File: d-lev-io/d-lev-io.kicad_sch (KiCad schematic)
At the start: 48 parts, among them J1 USB_C_Receptacle_USB2.0, J2 PJ-059A, J3 Conn_01x12_MountingPin, J4 MIDI_OUT_JACK, U3 ADP151-3.3, U6 74AHC1G126

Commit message: io board more analog schematic capture
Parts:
- added J6: HEADPHONE, Connector_Audio:Jack_3.5mm_CUI_SJ-3523-SMT_Horizontal, symbol Connector:AudioJack3
- added R42, R44: 0, Resistor_SMD:R_0603_1608Metric, symbol Device:R_Small
- added RV2: VOL_POT, symbol Device:R_Potentiometer_MountingPin
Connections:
- net +3V3: now also RV2.1
- net GND: now also RV2.3, RV2.MP (MountPin)
- new net: J6.R, R42.1
- new net: J6.T, R44.1
- new net OUT_SE.G: J6.S, R42.2, R44.2
- new net SAMD11/VOLUME_POT: RV2.2
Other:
- sheet DAC ports: added DAC_GPIO, DAC_RESET, HPA_SHDN, OUT_SE{L,R,G}; removed DAC{GPIO,RESET}, OUT_BAL{L+,L-,R+,R-}
- sheet SAMD11 ports: added ESS_GPIO, HPA_SHDN, VOLUME_POT; removed none
- note added: "hpa: MAX97220C/E"
- note removed: "hpa: MAX97220A"
- moved on the sheet: C21, C22, TP4, U3

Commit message: many board updates
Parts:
- removed JP3: JUMP_VBUCK, Jumper:SolderJumper-2_P1.3mm_Bridged_RoundedPad1.0x1.5mm, symbol Jumper:Jumper_2_Bridged
- removed JP4: JUMP_VBUS, Jumper:SolderJumper-2_P1.3mm_Bridged_RoundedPad1.0x1.5mm, symbol Jumper:Jumper_2_Bridged
- removed RV2: VOL_POT, symbol Device:R_Potentiometer_MountingPin
- added C22 (x2): 4.7n, Capacitor_SMD:C_0603_1608Metric, symbol Device:C_Small
- added C22 (x2): 100n, Capacitor_SMD:C_0603_1608Metric, symbol Device:C_Small
- added H1, H2, H4, H5: MountingHole_Pad, theremin:SMTSO-M3, symbol Mechanical:MountingHole_Pad
- added H3: MountingHole_Pad, theremin:MicStandHole, symbol Mechanical:MountingHole_Pad
- added R42 (x2): 75, Resistor_SMD:R_0603_1608Metric, symbol Device:R_Small
- added R42 (x2): 100k, Resistor_SMD:R_0603_1608Metric, symbol Device:R_Small
- added R42 (x2): 220, Resistor_SMD:R_0603_1608Metric, symbol Device:R_Small
- added TP25: VBUCK, TestPoint:TestPoint_Pad_D1.5mm, symbol Connector:TestPoint
- added U4: 74LVC2GU04, Package_TO_SOT_SMD:SOT-23-6, symbol 74xGxx:74LVC2GU04
- added VR1: RK09711110EL, theremin:RK09711110EL, symbol assorted:RK09711110EL
- R18: value 10 -> 220
- R42, R44: value 0 -> 27
- R8: value 33 -> 220
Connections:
- net VDD is gone; now on net +5V: C21.2, U3.1 (VIN), U3.3 (EN)
- net +3.3VA: now also C22.2, U4.5 (VCC)
- net +3V3: now also VR1.3 (CW); no longer R8.1, U6.1, U6.5 (VCC)
- net +5V: now also R8.1, U6.1, U6.5 (VCC), C22.2, VR1.4 (COM); no longer C2.2, C3.2, C4.2, C5.2, C6.2, C7.2, FB1.2
- net Buck/VOUT: now also TP25.1
- net GND: now also C22.1, C22.1, H1.1, H2.1, H3.1, H4.1, H5.1, R42.2, R42.2, U4.2 (GND), VR1.1 (CCW)
- net SAMD11/VOLUME_POT: now also VR1.2 (WIPER)
- net spdif_line: now also C22.2, R42.1
- net spdif_mon: now also C22.2, R42.1
- net UINN: now reaches J1.A7 (D-), J1.B7 (D-), R3.2
- net at D1.1 (K): now also D2.1 (K), FB1.1
- net UINP: now reaches J1.A6 (D+), J1.B6 (D+), R4.2
- removed net OUT_SE.G: J6.S, R42.2, R44.2
- net USB.DM renamed USB.DN
- new net: C22.1, R42.2 (x2)
- new net: R42.1, R42.1, U4.3
- new net: R42.1, R42.1, U4.1
- new net DAC/OUT_SE_G: J6.S
- new net DAC/OUT_SE_L: R44.2
- new net DAC/OUT_SE_R: R42.2
- new net SPDIF1: R42.2, U4.6
- new net SPDIF2: R42.2, U4.4
- new net SWITCH_LOW: C2.2, C3.2, C4.2, C5.2, C6.2, C7.2, FB1.2, VR1.5 (NO)
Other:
- sheet DAC ports: added OUT_SE_G, OUT_SE_L, OUT_SE_R; removed OUT_SE{L,R,G}
- sheet SAMD11 ports: added USB{DN,DP}; removed USB{DM,DP}
- moved on the sheet: C21, C22, FB1, J4, J6, R18, R42, R44, R8, U3, U6

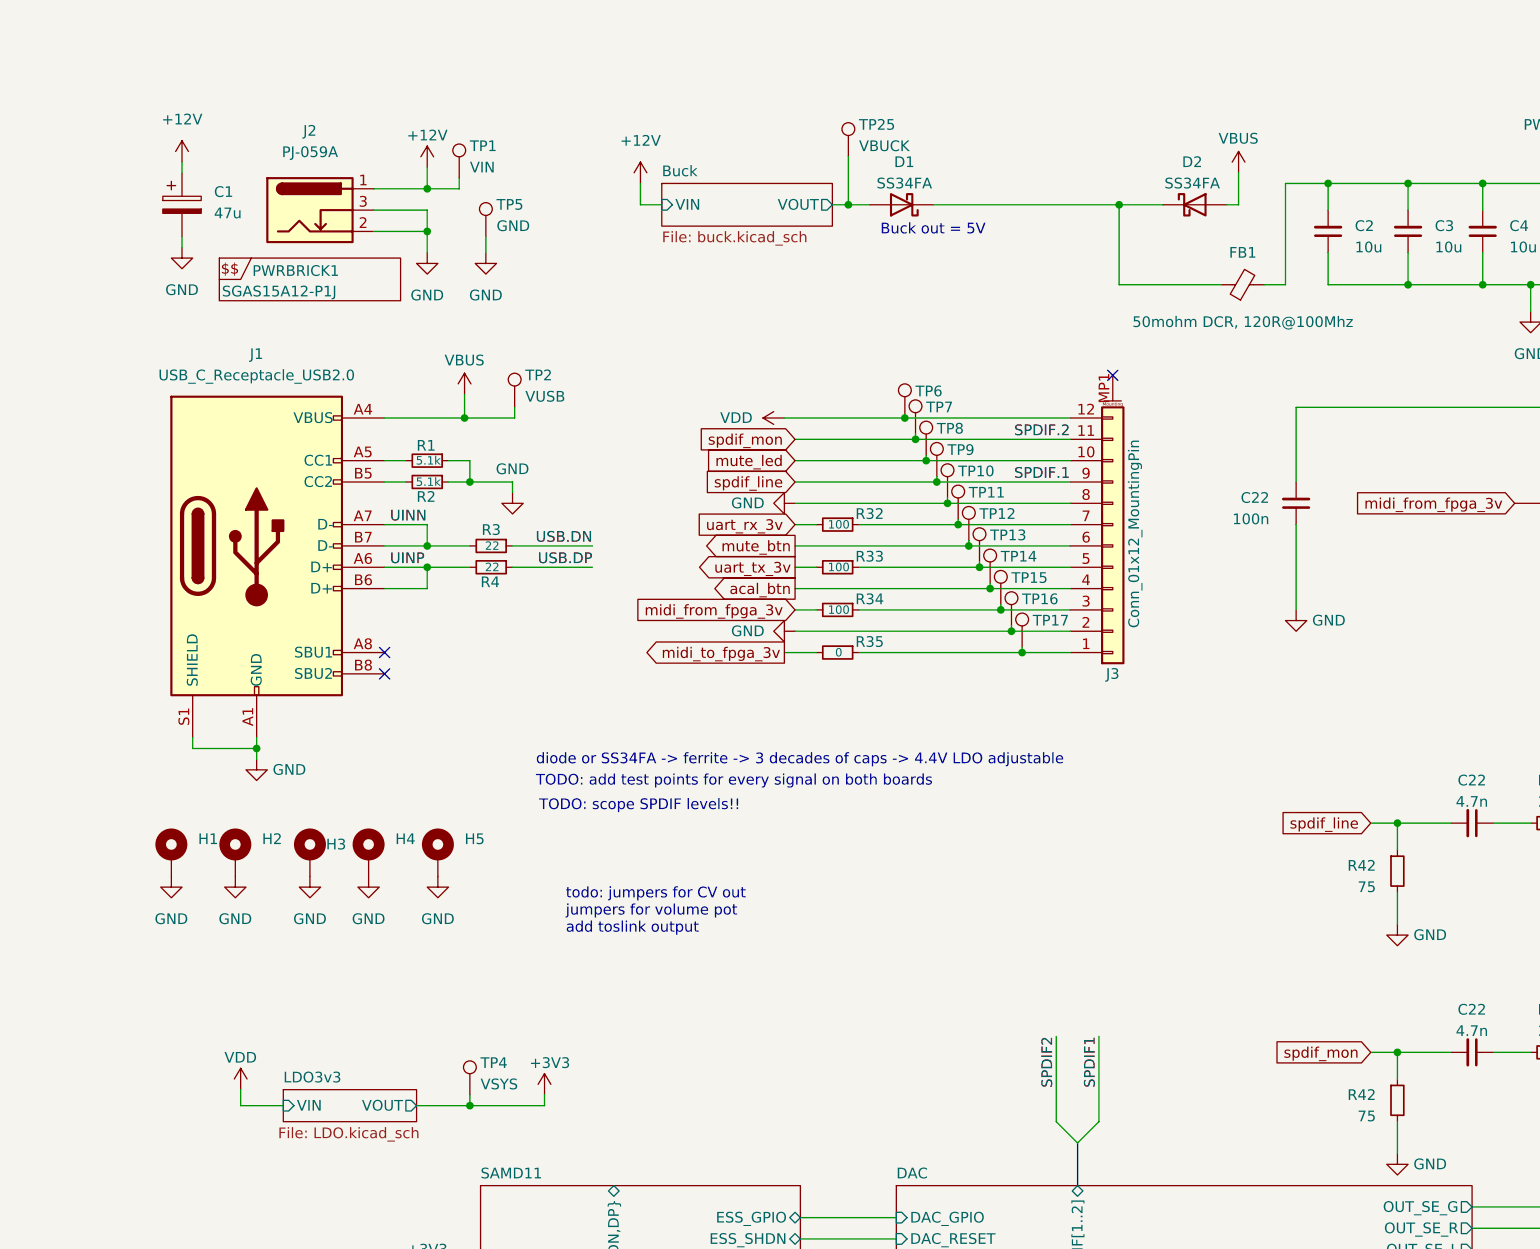
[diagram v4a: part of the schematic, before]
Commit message: Routed IO board
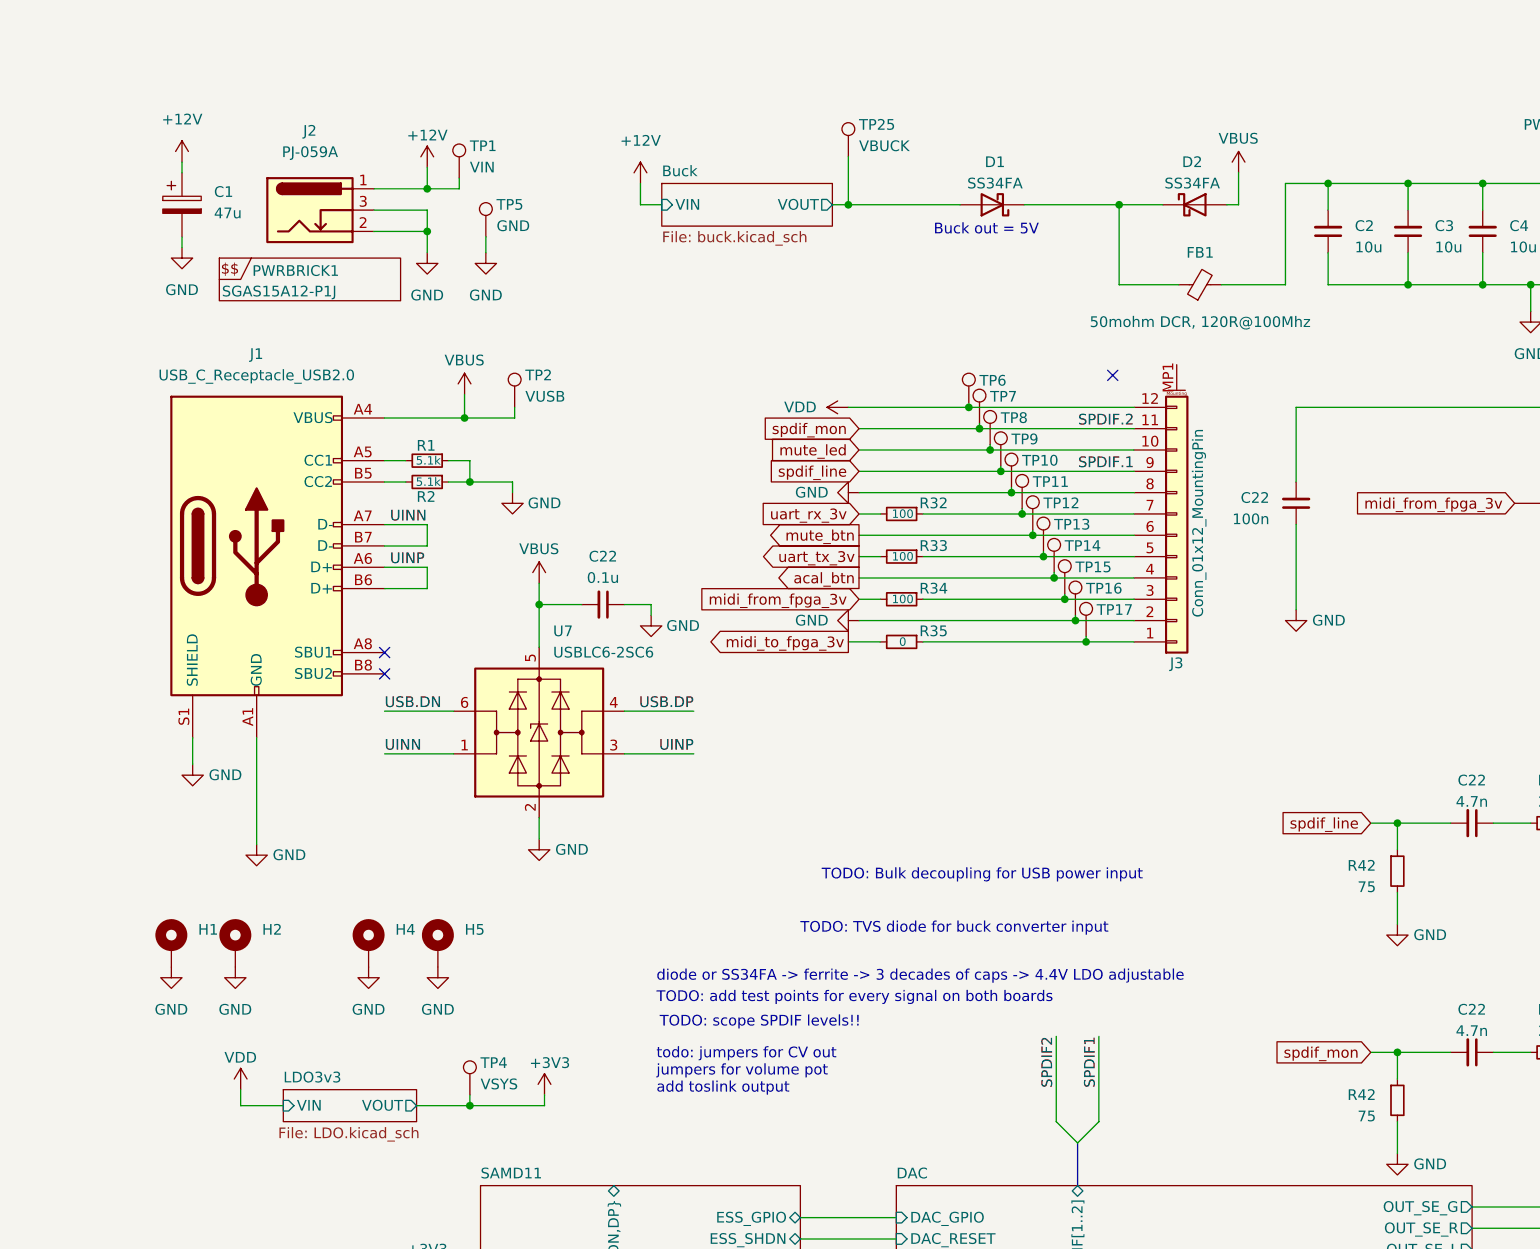
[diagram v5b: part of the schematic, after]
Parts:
- removed H3: MountingHole_Pad, theremin:MicStandHole, symbol Mechanical:MountingHole_Pad
- removed R3, R4: 22, Resistor_SMD:R_0603_1608Metric, symbol Device:R_Small
- added C22: 0.1u, Capacitor_SMD:C_0805_2012Metric, symbol Device:C_Small
- added U7: USBLC6-2SC6, Package_TO_SOT_SMD:SOT-23-6, symbol Power_Protection:USBLC6-2SC6
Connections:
- net GND: now also C22.1, U7.2 (GND)
- net UINN: now also U7.1 (I/O1)
- net UINP: now also U7.3 (I/O2)
- net USB.DN: now also U7.6 (I/O1)
- net USB.DP: now also U7.4 (I/O2)
- net VBUS: now also C22.2, U7.5 (VBUS)
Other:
- note added: "TODO: Bulk decoupling for USB power input"
- note added: "TODO: TVS diode for buck converter input"
- moved on the sheet: D1, FB1, H1, H2, H4, H5, J3, R32, R33, R34, R35, TP10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

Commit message: add 5-pin CV expansion header
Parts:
- added J8: CV_HDR, Connector_JST:JST_SH_SM05B-SRSS-TB_1x05-1MP_P1.00mm_Horizontal, symbol Connector_Generic:Conn_01x05
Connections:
- net +5V: now also J8.1 (Pin_1)
- net GND: now also J8.5 (Pin_5)
- new net SAMD11/CV_EN: J8.2 (Pin_2)
- new net SCL: J8.4 (Pin_4)
- new net SDA: J8.3 (Pin_3)
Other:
- sheet SAMD11 ports: added CV_EN; removed none
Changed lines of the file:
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@@
     (stroke (width 0) (type default))
   )
+  (wire (pts (xy 88.9 184.912) (xy 88.9 178.435))
+    (stroke (width 0) (type default))
+  )
   (polyline (pts (xy 133.35 -39.37) (xy 132.08 -38.1))
     (stroke (width 0) (type default))
@@
     (stroke (width 0) (type default))
   )
+  (wire (pts (xy 89.027 184.912) (xy 89.027 185.039))
+    (stroke (width 0) (type default))
+  )
   (wire (pts (xy 100.965 62.865) (xy 103.505 62.865))
     (stroke (width 0) (type default))
@@
     (stroke (width 0) (type default))
   )
+  (wire (pts (xy 94.996 185.039) (xy 89.027 185.039))
+    (stroke (width 0) (type default))
+  )
   (polyline (pts (xy 135.89 -36.83) (xy 137.16 -38.1))
     (stroke (width 0) (type default))
@@
     (stroke (width 0) (type default))
   )
+  (wire (pts (xy 94.996 187.579) (xy 66.167 187.579))
+    (stroke (width 0) (type default))
+  )
   (polyline (pts (xy 245.745 -42.926) (xy 244.475 -44.196))
     (stroke (width 0) (type default))
@@
     (stroke (width 0) (type default))
   )
+  (wire (pts (xy 94.996 180.594) (xy 94.996 182.499))
+    (stroke (width 0) (type default))
+  )
   (wire (pts (xy 20.32 22.225) (xy 20.32 20.955))
     (stroke (width 0) (type default))
@@
     (stroke (width 0) (type default))
   )
+  (wire (pts (xy 73.787 193.929) (xy 73.787 192.659))
+    (stroke (width 0) (type default))
+  )
   (wire (pts (xy 54.61 133.35) (xy 63.5 133.35))
     (stroke (width 0) (type default))
@@
     (stroke (width 0) (type default))
   )
+  (wire (pts (xy 94.996 192.659) (xy 73.787 192.659))
+    (stroke (width 0) (type default))
+  )
   (wire (pts (xy 247.65 117.475) (xy 247.65 127.635))
     (stroke (width 0) (type default))
@@
     (stroke (width 0) (type default))
   )
+  (wire (pts (xy 89.027 184.912) (xy 88.9 184.912))
+    (stroke (width 0) (type default))
+  )
   (wire (pts (xy 166.37 159.385) (xy 160.655 159.385))
     (stroke (width 0) (type default))
@@
     (stroke (width 0) (type default))
   )
+  (wire (pts (xy 94.996 190.119) (xy 66.167 190.119))
+    (stroke (width 0) (type default))
+  )
   (wire (pts (xy 53.975 51.435) (xy 59.944 51.435))
     (stroke (width 0) (type default))
@@
     (effects (font (size 1.27 1.27)) (justify left bottom))
   )
+  (label "SDA" (at 66.167 187.579 0) (fields_autoplaced)
+    (effects (font (size 1.27 1.27)) (justify left bottom))
+  )
   (label "SPDIF1" (at 129.54 125.095 270) (fields_autoplaced)
     (effects (font (size 1.27 1.27)) (justify right bottom))
@@
     (effects (font (size 1.27 1.27)) (justify right bottom))
   )
+  (label "SCL" (at 66.167 190.119 0) (fields_autoplaced)
+    (effects (font (size 1.27 1.27)) (justify left bottom))
+  )
   (label "UINN" (at 45.085 64.135 0) (fields_autoplaced)
     (effects (font (size 1.27 1.27)) (justify left bottom))
@@
     )
   )
+  (symbol (lib_id "power:+5V") (at 94.996 180.594 0) (unit 1)
+    (in_bom yes) (on_board yes) (dnp no) (fields_autoplaced)
+    (property "Reference" "#PWR078" (at 94.996 184.404 0)
+      (effects (font (size 1.27 1.27)) hide)
+    )
+    (property "Value" "VDD" (at 94.996 176.784 0)
+      (effects (font (size 1.27 1.27)))
+    )
+    (property "Footprint" "" (at 94.996 180.594 0)
+      (effects (font (size 1.27 1.27)) hide)
+    )
+    (property "Datasheet" "" (at 94.996 180.594 0)
+      (effects (font (size 1.27 1.27)) hide)
+    )
+    (pin "1")
+    (instances
+      (project "d-lev-io"
+        (path "/9261a07b-ae4a-4d72-8042-ea097cd0e5ed"
+          (reference "#PWR078") (unit 1)
+        )
+      )
+    )
+  )
   (symbol (lib_id "Device:R_Small") (at 183.515 127 270) (unit 1)
     (in_bom yes) (on_board yes) (dnp no) (fields_autoplaced)
@@
     )
   )
+  (symbol (lib_id "power:GND") (at 73.787 193.929 0) (unit 1)
+    (in_bom yes) (on_board yes) (dnp no) (fields_autoplaced)
+    (property "Reference" "#PWR026" (at 73.787 200.279 0)
+      (effects (font (size 1.27 1.27)) hide)
+    )
+    (property "Value" "GND" (at 73.787 199.009 0)
+      (effects (font (size 1.27 1.27)))
+    )
+    (property "Footprint" "" (at 73.787 193.929 0)
+      (effects (font (size 1.27 1.27)) hide)
+    )
+    (property "Datasheet" "" (at 73.787 193.929 0)
+      (effects (font (size 1.27 1.27)) hide)
+    )
+    (pin "1")
+    (instances
+      (project "d-lev-io"
+        (path "/9261a07b-ae4a-4d72-8042-ea097cd0e5ed"
+          (reference "#PWR026") (unit 1)
+        )
+        (path "/9261a07b-ae4a-4d72-8042-ea097cd0e5ed/fd6a6c10-f456-4937-8c5d-f097bbb805c0"
+          (reference "#PWR026") (unit 1)
+        )
+      )
+      (project "dlev-mini"
+        (path "/eb5e8bfd-9871-4528-bf57-58851bf63907/6062d07e-a4ed-44ac-a6b0-014aac464169"
+          (reference "#PWR0139") (unit 1)
+        )
+      )
+    )
+  )
   (symbol (lib_id "Connector:TestPoint") (at 120.396 62.23 0) (unit 1)
     (in_bom yes) (on_board yes) (dnp no)
@@
     )
   )
+  (symbol (lib_id "Connector_Generic:Conn_01x05") (at 100.076 187.579 0) (unit 1)
+    (in_bom yes) (on_board yes) (dnp no) (fields_autoplaced)
+    (property "Reference" "J8" (at 102.616 186.944 0)
+      (effects (font (size 1.27 1.27)) (justify left))
+    )
+    (property "Value" "CV_HDR" (at 102.616 189.484 0)
+      (effects (font (size 1.27 1.27)) (justify left))
+    )
+    (property "Footprint" "Connector_JST:JST_SH_SM05B-SRSS-TB_1x05-1MP_P1.00mm_Horizontal" (at 100.076 187.579 0)
+      (effects (font (size 1.27 1.27)) hide)
+    )
+    (property "Datasheet" "~" (at 100.076 187.579 0)
+      (effects (font (size 1.27 1.27)) hide)
+    )
+    (property "Tolerance" "" (at 100.076 187.579 0)
+      (effects (font (size 1.27 1.27)))
+    )
+    (pin "1")
+    (pin "2")
+    (pin "3")
+    (pin "4")
+    (pin "5")
+    (instances
+      (project "d-lev-io"
+        (path "/9261a07b-ae4a-4d72-8042-ea097cd0e5ed/fd6a6c10-f456-4937-8c5d-f097bbb805c0"
+          (reference "J8") (unit 1)
+        )
+        (path "/9261a07b-ae4a-4d72-8042-ea097cd0e5ed"
+          (reference "J8") (unit 1)
+        )
+      )
+    )
+  )
   (symbol (lib_id "power:GND") (at 165.1 111.76 0) (unit 1)
     (in_bom yes) (on_board yes) (dnp no) (fields_autoplaced)
@@
       (effects (font (size 1.27 1.27)) (justify right))
     )
+    (pin "CV_EN" output (at 88.9 178.435 270)
+      (effects (font (size 1.27 1.27)) (justify left))
+    )
     (instances

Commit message: route cv header
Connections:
- net SCL: now also J8.3 (Pin_3); no longer J8.4 (Pin_4)
- net SDA: now also J8.4 (Pin_4); no longer J8.3 (Pin_3)
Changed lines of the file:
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@@
     (effects (font (size 1.27 1.27)) (justify left bottom))
   )
-  (label "SDA" (at 66.167 187.579 0) (fields_autoplaced)
+  (label "SDA" (at 66.167 190.119 0) (fields_autoplaced)
     (effects (font (size 1.27 1.27)) (justify left bottom))
   )
@@
     (effects (font (size 1.27 1.27)) (justify right bottom))
   )
-  (label "SCL" (at 66.167 190.119 0) (fields_autoplaced)
+  (label "SCL" (at 66.167 187.579 0) (fields_autoplaced)
     (effects (font (size 1.27 1.27)) (justify left bottom))
   )

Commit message: I/O board silk placement
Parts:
- added TP11, TP7, TP8: VUSB, TestPoint:TestPoint_Pad_D1.5mm, symbol Connector:TestPoint
- added TP39: VDD_B4SW, TestPoint:TestPoint_Pad_D1.5mm, symbol Connector:TestPoint
- renumbered C5 to C22, C3 to C24, C6 to C28, C2 to C30, C7 to C32, C4 to C33, C1 to C41, D2 to D1, D1 to D2, H4 to H1, H5 to H3, H1 to H4, J4 to J2, J1 to J3, J3 to J4, J2 to J5, R8 to R1, R32 to R10, R33 to R14, R35 to R15, R34 to R17, R18 to R24, R1 to R3, R2 to R4, TP1 to TP13, TP2 to TP14, TP25 to TP15, TP4 to TP2, TP9 to TP27, TP15 to TP28, TP8 to TP29, TP12 to TP30, TP13 to TP31, TP6 to TP32, TP7 to TP33, TP14 to TP34, TP16 to TP35, TP10 to TP36, TP17 to TP37, TP11 to TP38, TP5 to TP4, U4 to U1, U6 to U3, U7 to U6
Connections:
- net SPDIF1: now also TP8.1
- net SPDIF2: now also TP7.1
- net SWITCH_LOW: now also TP39.1
- net at R24.1, U3.4: now also TP11.1
